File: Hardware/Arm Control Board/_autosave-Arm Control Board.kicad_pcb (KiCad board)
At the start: 2 copper layers, 99 parts, among them P1 Servo 1, P10 UIM240XX_Stepper_Conn, P11 Battery, P12 SyRen, P13 Raspberry Pi, P2 Shoulder Feedback, P3 Servo 2, P4 Servo 3, P5 Elbow Feedback, P6 Servo 4, P7 RS485, P8 ST_SWD_Connector, P9 Servo 5, U1 STM32F401RCT6, U2 SN75176BDR, U3 74LVCH244APW, U4 AOZ1280CI, U5 AOZ1280CI, U6 AP65552SP-13, U7 AP65552SP-13, U8 AP65552SP-13, U9 AP65552SP-13, X1 24MHz

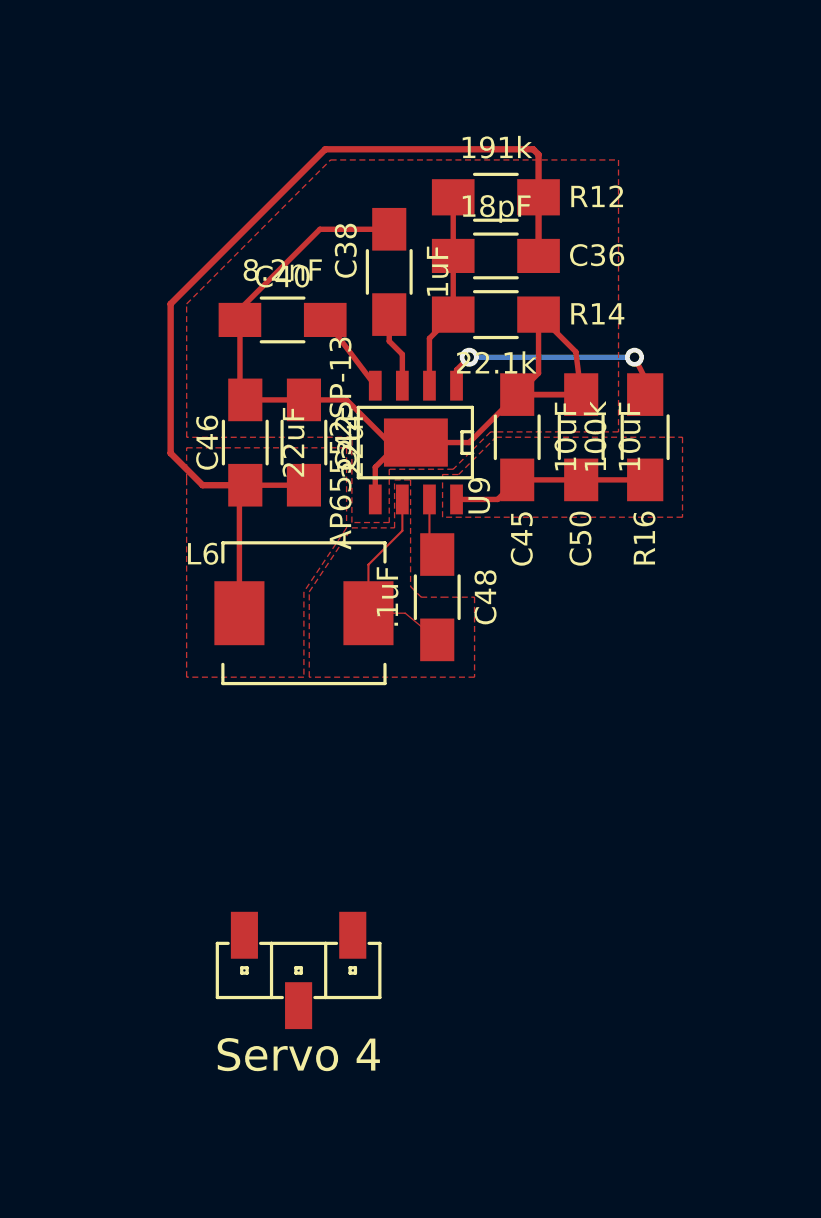
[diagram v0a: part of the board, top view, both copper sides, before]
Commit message: reg4 converted to datasheet recommended layout
it's kind of crazy i didn't think to look there first before I created
three of my own
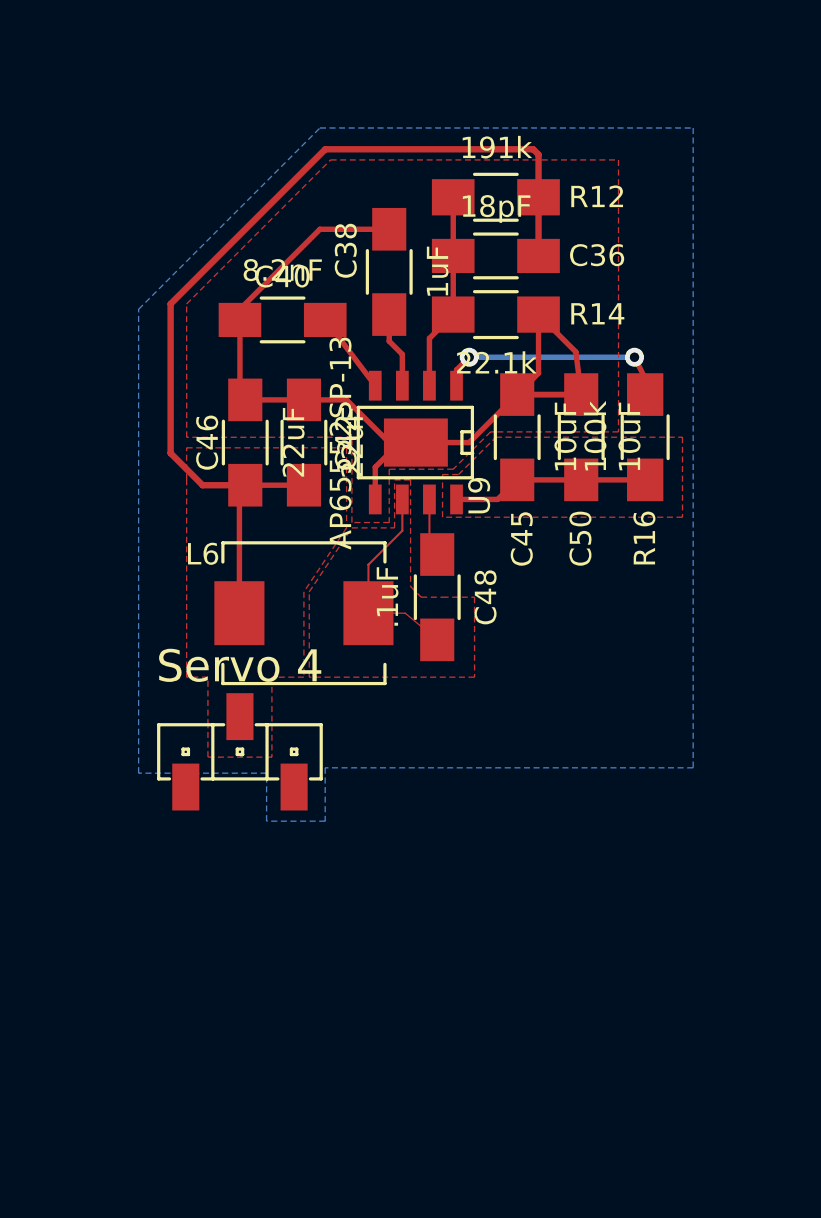
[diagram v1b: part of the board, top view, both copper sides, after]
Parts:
- moved P6 10.6 mm to (100.2, 153.8), turned to 180 degrees
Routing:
- added copper zone on B.Cu, net GND
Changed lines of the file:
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@@
   (general
     (links 237)
-    (no_connects 143)
+    (no_connects 142)
     (area -85.462333 -13.479 352.410859 242.079001)
     (thickness 1.6)
@@
   )
   (module MAVRIC_footprints:1x3_SMD_header (layer F.Cu)
-    (at 103 164)
-    (fp_text reference P6 (at 0 -4) (layer F.SilkS) hide
+    (at 100.25 153.75 180)
+    (fp_text reference P6 (at 0 -4 180) (layer F.SilkS) hide
       (effects (font (size 1.5 1.5) (thickness 0.15)))
     )
-    (fp_text value "Servo 4" (at 0 4) (layer F.SilkS)
+    (fp_text value "Servo 4" (at 0 4 180) (layer F.SilkS)
       (effects (font (size 1.5 1.5) (thickness 0.15)))
     )
@@
     (fp_line (start -2.413 0.127) (end -2.413 -0.127) (layer F.SilkS) (width 0.15))
     (fp_line (start -2.413 -0.127) (end -2.667 -0.127) (layer F.SilkS) (width 0.15))
-    (pad 2 smd rect (at 0 1.65) (size 1.27 2.2) (layers F.Cu F.Paste F.Mask)
+    (pad 2 smd rect (at 0 1.65 180) (size 1.27 2.2) (layers F.Cu F.Paste F.Mask)
       (net 27 "/7.4V Regulators/REG4+7V4"))
-    (pad 1 smd rect (at -2.54 -1.65) (size 1.27 2.2) (layers F.Cu F.Paste F.Mask)
+    (pad 1 smd rect (at -2.54 -1.65 180) (size 1.27 2.2) (layers F.Cu F.Paste F.Mask)
       (net 2 GND))
-    (pad 3 smd rect (at 2.54 -1.65) (size 1.27 2.2) (layers F.Cu F.Paste F.Mask)
+    (pad 3 smd rect (at 2.54 -1.65 180) (size 1.27 2.2) (layers F.Cu F.Paste F.Mask)
       (net 89 /Servo4_PWM))
   )
@@
     (polygon
       (pts
-        (xy 105.25 143.25) (xy 103.25 146.25) (xy 103.25 150.25) (xy 97.75 150.25) (xy 97.75 143.5)
+        (xy 105.25 143.25) (xy 103.25 146.25) (xy 103.25 150.25) (xy 101.75 150.25) (xy 101.75 154)
+        (xy 98.75 154) (xy 98.75 152.5) (xy 98.75 150.25) (xy 97.75 150.25) (xy 97.75 143.5)
         (xy 97.75 141) (xy 97.75 139.496) (xy 105.25 139.496)
       )
@@
       )
     )
+  )
+  (zone (net 2) (net_name GND) (layer B.Cu) (hatch edge 0.508)
+    (connect_pads (clearance 0.2))
+    (min_thickness 0.2)
+    (fill yes (arc_segments 16) (thermal_gap 0.508) (thermal_bridge_width 0.508))
+    (polygon
+      (pts
+        (xy 104 124.5) (xy 121.5 124.5) (xy 121.5 154.5) (xy 104.25 154.5) (xy 104.25 157)
+        (xy 101.5 157) (xy 101.5 154.75) (xy 95.5 154.75) (xy 95.5 133) (xy 104 124.5)
+      )
+    )
